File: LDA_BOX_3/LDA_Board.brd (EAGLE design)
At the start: 78 x 55 mm, 65 parts, among them IC1 STM32F407ZET, SW3P-2 LD-CCB-001, Y1 8MHZ

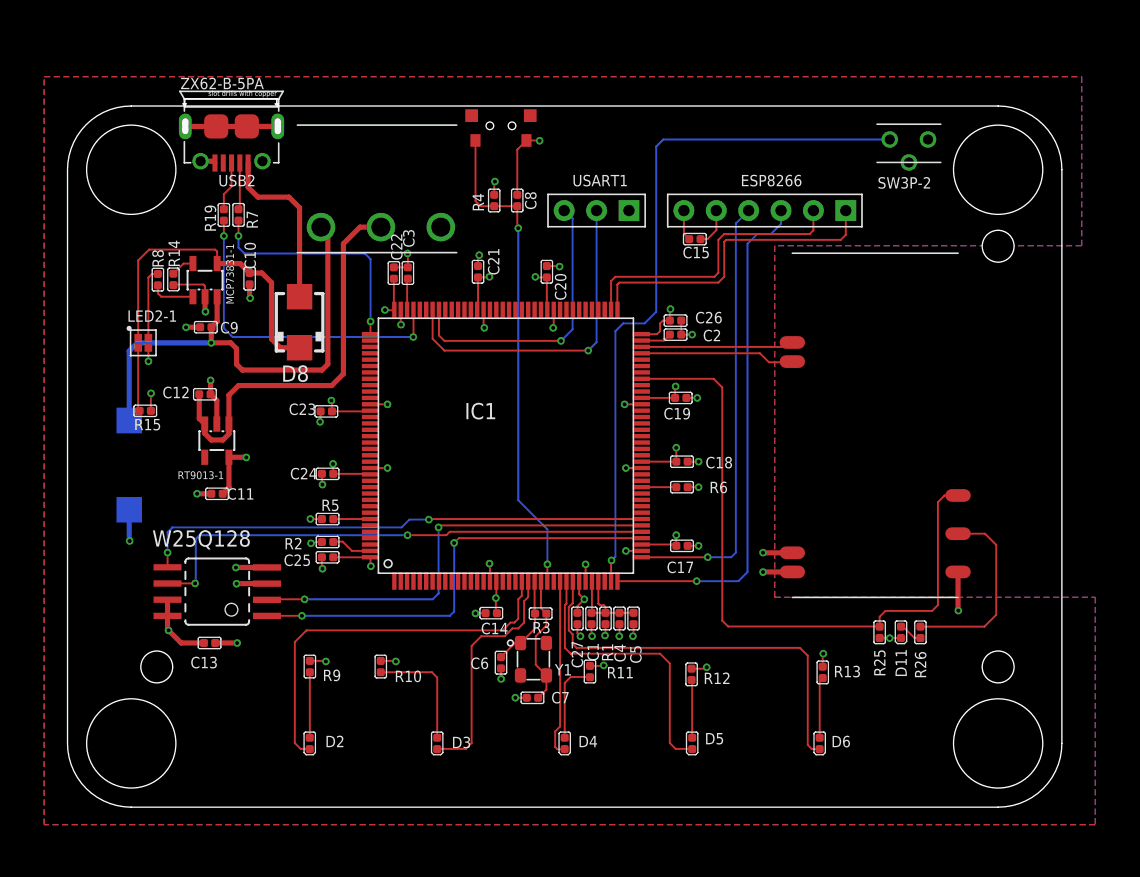
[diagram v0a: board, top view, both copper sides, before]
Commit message: 第三版盒子，丝印加了logo
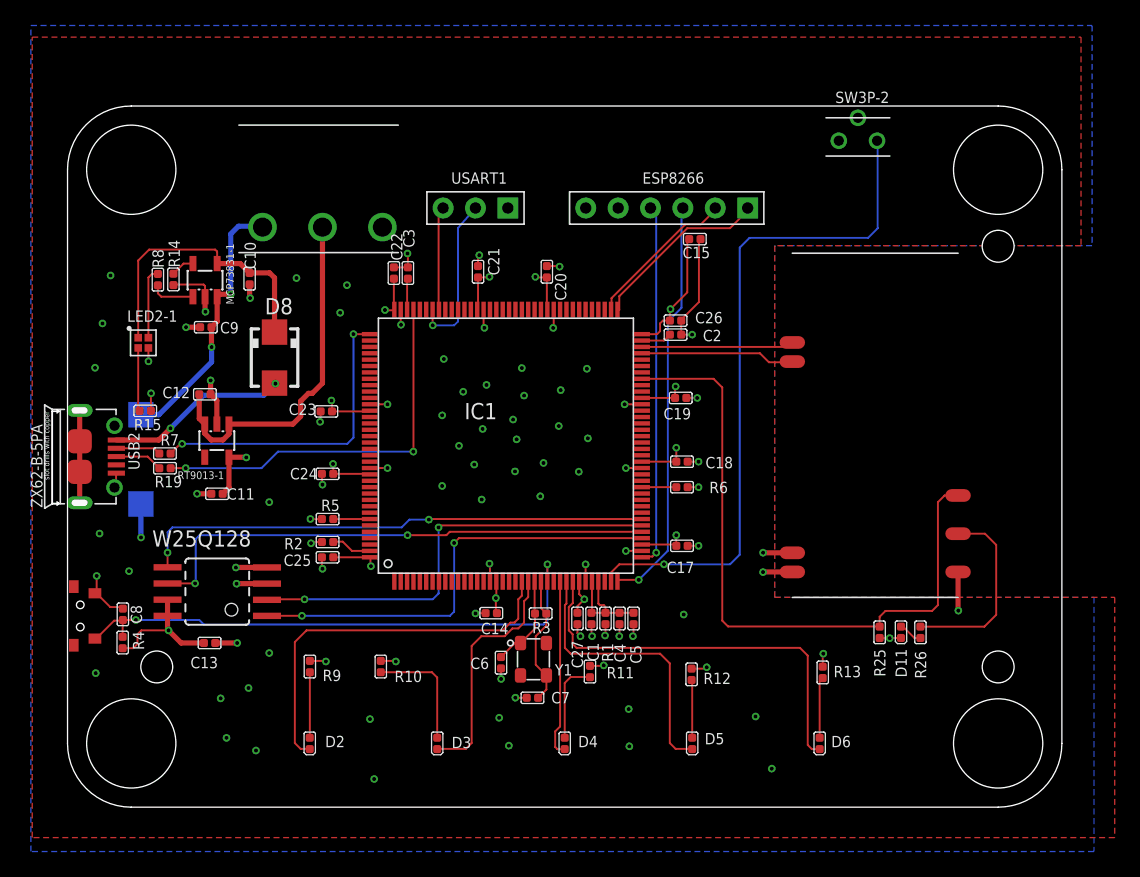
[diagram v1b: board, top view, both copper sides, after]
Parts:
- C1, C2, C3: value 225 -> 15pf
- C10, C9: value 4.7uf -> 15pf
- C11: value 1uf -> 15pf
- C12, C4: value 10uf -> 15pf
- C13, C14, C15, C17, C18, C19, C20, C21, C22, C23, C24, C25, C26, C27, C5, C8: value 104 -> 15pf
- C6, C7: value 22pf -> 15pf
- R10, R11, R12, R13, R9: value 510R -> 0R
- R14: value 2k -> 0R
- R15, R8: value 470R -> 0R
- R25, R4: value 10k -> 0R
- R26: value 1.5k -> 0R
- R3: value 1M -> 0R
- moved B-1 50.7 mm to (1.00, 15.0), turned to 270 degrees
- moved R4 45.3 mm to (4.33, 12.9), turned to 0 degrees
- moved C8 44.8 mm to (4.34, 15.1)
- moved USB2 28.5 mm to (0.96, 27.5), turned to 270 degrees
- moved R19 20.4 mm to (7.64, 26.6), turned to 90 degrees
- moved R7 19.6 mm to (7.64, 27.7), turned to 90 degrees
- moved USART1 9.50 mm to (32.0, 47.0)
- moved ESP8266 7.70 mm to (47.0, 47.0)
- moved SW3P-2 5.32 mm to (62.0, 54.1), turned to 0 degrees
- moved SW-1 4.58 mm to (20.0, 45.5)
- moved D8 3.40 mm to (16.2, 35.3), turned to 270 degrees
- moved BATTERY-1 1.02 mm to (4.75, 31.8)
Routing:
- net BATTERY: track 37.9 -> 21.2 mm, vias 1 -> 2
- net TX1: track 22.6 -> 8.16 mm, vias 1 -> 0
- net RX1: track 26.1 -> 12.7 mm
- net GBC_LED: track 25.1 -> 14.3 mm
- net GBC_KEY: track 22.9 -> 12.1 mm
- net TX2: track 40.6 -> 32.3 mm
- net +3V3: track 69.4 -> 76.9 mm, vias 25 -> 24
- net RX2: track 34.8 -> 28.5 mm
- net CLK: track 18.7 -> 24.3 mm
- net RESET: track 38.6 -> 43.6 mm
- net SWD: track 25.7 -> 30.7 mm
- net +3.7V: track 32.0 -> 27.9 mm
- net GND: track 75.9 -> 78.6 mm, vias 42 -> 87
- net +5V: track 25.4 -> 22.8 mm
- net KEY1: track 55.1 -> 53.8 mm
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- added copper zone on layer 1, net GND
- added copper zone on layer 16, net GND
- removed copper zone on layer 1, net N$10
- removed copper zone on layer 16, net N$12
